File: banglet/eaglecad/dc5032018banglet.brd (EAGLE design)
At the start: 39.8 x 22.6 mm, 40 parts, among them Q3 DMG3415U-7, U2 AP2112(3.3V), U3 MCP73831T-2ACI/OT, U4 CP2104, X1 32.768, X2 JSTPH, X4 20329

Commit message: Connect the unconnected; add in a junction
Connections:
- new net DIO/P0.17: U1.P35
- new net TRACED0: U1.P36
- new net TRACED1: U1.P34
- new net TRACED2: U1.P33
- new net TRACED3: U1.P32
- net RESET: now also U1.P39
- net SWCLK: now also U1.P43
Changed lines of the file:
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@@
 <?xml version="1.0" encoding="utf-8"?>
 <!DOCTYPE eagle SYSTEM "eagle.dtd">
-<eagle version="8.2.1">
+<eagle version="8.6.3">
 <drawing>
 <settings>
 <setting alwaysvectorfont="no"/>
+<setting keepoldvectorfont="yes"/>
 <setting verticaltext="up"/>
 </settings>
@@
 <layer number="59" name="tCarbon" color="7" fill="1" visible="no" active="no"/>
 <layer number="60" name="bCarbon" color="7" fill="1" visible="no" active="no"/>
-<layer number="88" name="SimResults" color="7" fill="1" visible="yes" active="yes"/>
-<layer number="89" name="SimProbes" color="7" fill="1" visible="yes" active="yes"/>
+<layer number="88" name="SimResults" color="7" fill="1" visible="no" active="no"/>
+<layer number="89" name="SimProbes" color="7" fill="1" visible="no" active="no"/>
 <layer number="90" name="Modules" color="5" fill="1" visible="no" active="no"/>
 <layer number="91" name="Nets" color="2" fill="1" visible="no" active="no"/>
@@
 <param name="dpMaxLengthDifference" value="10mm"/>
 <param name="dpGapFactor" value="2.5"/>
-<param name="checkGrid" value="0"/>
 <param name="checkAngle" value="0"/>
 <param name="checkFont" value="1"/>
 <param name="checkRestrict" value="1"/>
+<param name="checkStop" value="0"/>
+<param name="checkValues" value="0"/>
 <param name="useDiameter" value="13"/>
 <param name="maxErrors" value="50"/>
@@
 <wire x1="36.8046" y1="33.8328" x2="36.83" y2="33.782" width="0.1524" layer="1"/>
 <wire x1="14.0208" y1="48.768" x2="13.97" y2="48.768" width="0.1524" layer="1"/>
+<contactref element="U1" pad="P39"/>
+<wire x1="7.92" y1="45.622" x2="8.636" y2="47.664" width="0" layer="19" extent="1-1"/>
 </signal>
 <signal name="DTR">
@@
 <signal name="SWCLK">
 <contactref element="SWD" pad="4"/>
+<contactref element="U1" pad="P43"/>
+<wire x1="5.72" y1="45.622" x2="6.096" y2="51.943" width="0" layer="19" extent="1-1"/>
 </signal>
 <signal name="A0">
@@
 <signal name="N$7">
 </signal>
+<signal name="TRACED0">
+<contactref element="U1" pad="P36"/>
+</signal>
+<signal name="TRACED3">
+<contactref element="U1" pad="P32"/>
+</signal>
+<signal name="TRACED2">
+<contactref element="U1" pad="P33"/>
+</signal>
+<signal name="TRACED1">
+<contactref element="U1" pad="P34"/>
+</signal>
+<signal name="DIO/P0.17">
+<contactref element="U1" pad="P35"/>
+</signal>
 </signals>
 </board>
@@
 </note>
 <note version="8.2" severity="warning">
-Since Version 8.2, Eagle supports online libraries. The ids
+Since Version 8.2, EAGLE supports online libraries. The ids
 of those online libraries will not be understood (or retained)
 with this version.

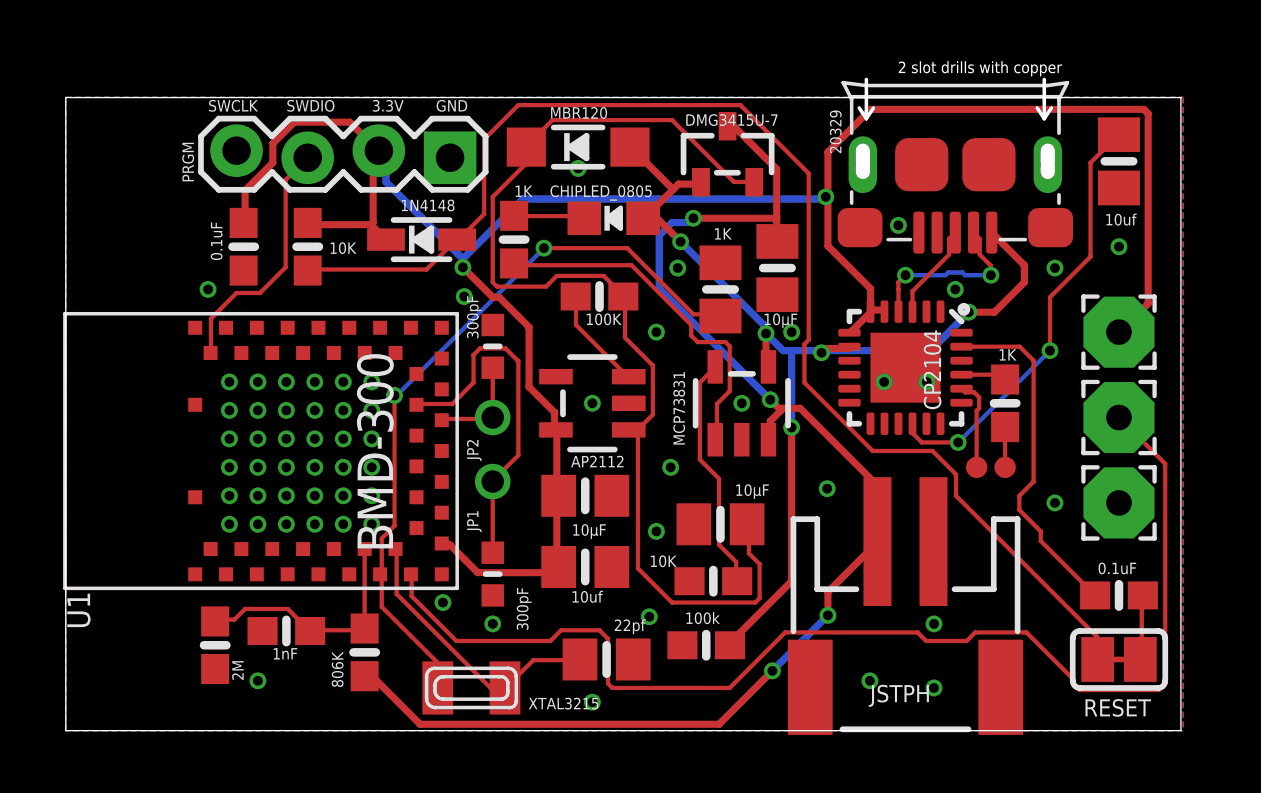
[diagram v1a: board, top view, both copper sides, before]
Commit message: connect uart tx/rx to bmd-300
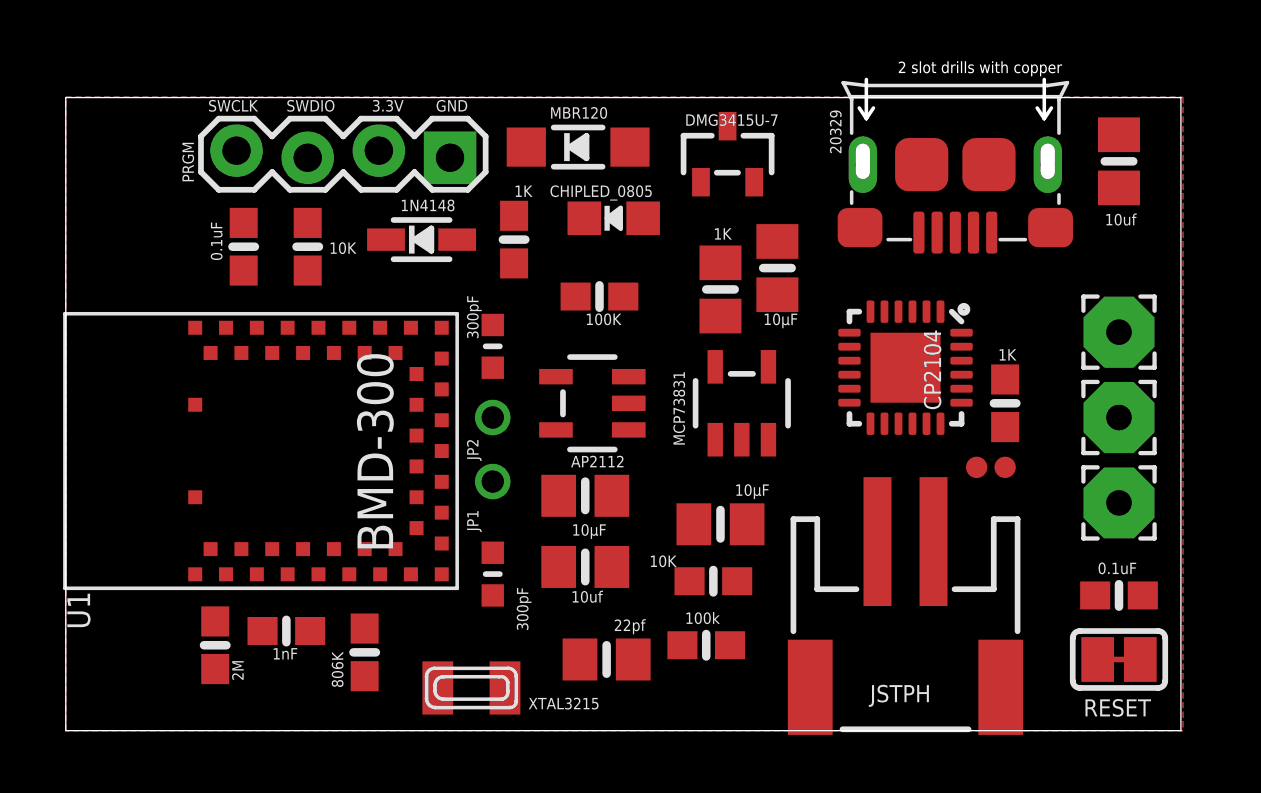
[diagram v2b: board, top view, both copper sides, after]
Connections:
- removed net N$3: R9.2, TP1.P$1
- removed net N$5: TP2.P$1, U4.20
- new net BDRX: R9.2, TP1.P$1, U1.P24
- new net BDTX: TP2.P$1, U1.P22, U4.20
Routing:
- net 3.3V: track 78.4 -> 0.00 mm, vias 2 -> 0
- net VBAT: track 47.6 -> 0.00 mm, vias 4 -> 0
- net RESET: track 45.9 -> 0.00 mm
- net A0: track 42.6 -> 0.00 mm
- net VIN: track 38.8 -> 0.00 mm
- net VBUS: track 37.7 -> 0.00 mm, vias 5 -> 0
- net N$2: track 26.4 -> 0.00 mm, vias 2 -> 0
- net N$14: track 15.5 -> 0.00 mm, vias 2 -> 0
- net N$9: track 12.7 -> 0.00 mm
- net DTR: track 12.5 -> 0.00 mm
- net N$6: track 12.4 -> 0.00 mm
- net N$1: track 9.99 -> 0.00 mm
- net SWDIO: track 8.90 -> 0.00 mm
- net A7/P0.31: track 8.79 -> 0.00 mm
- net N$10: track 8.45 -> 0.00 mm
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
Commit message: changed layout to perhaps better/easier routing.  Routed.
Opinions saught.
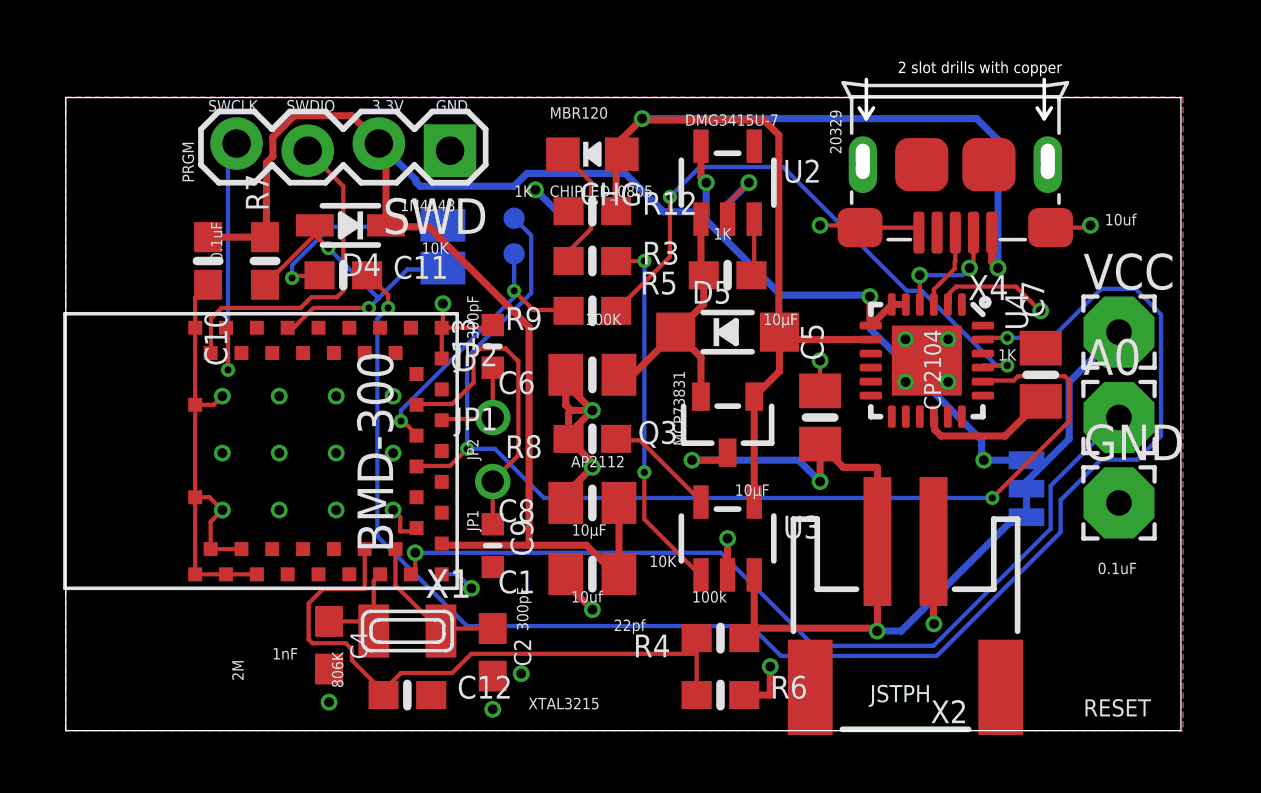
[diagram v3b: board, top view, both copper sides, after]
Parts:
- removed C3: 22pf, microbuilder:0805-NO
- added C4: 22pF, SparkFun-Capacitors:0603
- added JP3: JUMPER-SMT_3_1-NC_TRACE_SILK, SparkFun-Jumpers:SMT-JUMPER_3_1-NC_TRACE_SILK
- C2: value 22pf -> 22pF; device microbuilder:0805-NO -> SparkFun-Capacitors:0603
- moved C11 30.0 mm to (9.91, 47.5), turned to 0 degrees
- moved SJ2 28.3 mm to (13.5, 48.5), flipped to the bottom, turned to 90 degrees
- moved TP1 19.1 mm to (16.0, 48.3), flipped to the bottom
- moved TP2 18.8 mm to (16.0, 49.5), flipped to the bottom
- moved R6 18.1 mm to (23.4, 32.5), turned to 0 degrees
- moved R12 16.0 mm to (18.8, 49.8)
- moved C2 15.3 mm to (15.2, 34.0)
- moved R9 15.1 mm to (18.8, 46.2), turned to 180 degrees
- moved R4 12.7 mm to (23.4, 34.5), turned to 180 degrees
- moved Q3 9.65 mm to (23.6, 42.2), turned to 180 degrees
- moved U2 9.24 mm to (23.6, 50.8), turned to 0 degrees
- moved D5 8.49 mm to (23.6, 45.5)
- moved C7 8.12 mm to (34.8, 43.9), turned to 90 degrees
- moved C6 7.03 mm to (18.8, 43.9)
- moved R8 6.67 mm to (18.8, 41.7)
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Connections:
- new net N$3: JP3.2, VCC.1
- net 3.3V: now also JP3.1; no longer VCC.1
- net GND: now also C2.2, C4.2; no longer C2.1, C3.1
- net N$1: now also C2.1; no longer C3.2
- net N$2: now also C4.1; no longer C2.2
- net VBAT: now also JP3.3
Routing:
- net 3.3V: track 0.00 -> 71.6 mm, vias 0 -> 3
- net GND: track 0.00 -> 56.4 mm, vias 0 -> 33
- net DTR: track 0.00 -> 55.3 mm, vias 0 -> 2
- net VBUS: track 0.00 -> 44.6 mm, vias 0 -> 2
- net BDTX: track 0.00 -> 39.5 mm, vias 0 -> 2
- net A0: track 0.00 -> 31.6 mm, vias 0 -> 1
- net VBAT: track 0.00 -> 30.2 mm, vias 0 -> 3
- net A7/P0.31: track 0.00 -> 22.6 mm
- net N$11: track 0.00 -> 21.2 mm, vias 0 -> 2
- net N$9: track 0.00 -> 13.1 mm, vias 0 -> 2
- net RESET: track 0.00 -> 12.8 mm, vias 0 -> 2
- net SWDIO: track 0.00 -> 11.9 mm
- net N$6: track 0.00 -> 11.4 mm
- net BDRX: track 0.00 -> 10.7 mm, vias 0 -> 2
- net VIN: track 0.00 -> 9.82 mm
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
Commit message: add 2 fiducials
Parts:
- added FD1, FD2: FIDUCIALUFIDUCIAL, SparkFun-Aesthetics:FIDUCIAL-MICRO
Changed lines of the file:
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@@
 <attribute name="PROD_ID" value="CAP-07876" x="15.24" y="34.036" size="1.778" layer="27" rot="R270" display="off"/>
 </element>
+<element name="FD1" library="SparkFun-Aesthetics" library_urn="urn:adsk.eagle:library:507" package="FIDUCIAL-MICRO" package3d_urn="urn:adsk.eagle:package:37111/1" value="FIDUCIALUFIDUCIAL" x="5.334" y="32.004"/>
+<element name="FD2" library="SparkFun-Aesthetics" library_urn="urn:adsk.eagle:library:507" package="FIDUCIAL-MICRO" package3d_urn="urn:adsk.eagle:package:37111/1" value="FIDUCIALUFIDUCIAL" x="39.116" y="53.086"/>
 </elements>
 <signals>
